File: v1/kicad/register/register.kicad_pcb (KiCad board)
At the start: 2 copper layers, 78.5 x 66.5 mm, 5 parts, among them J3 ASYNC_{out}, U1 74HC173, U2 74HC173, U3 74LS244, U5 LNCPU Type B Connector

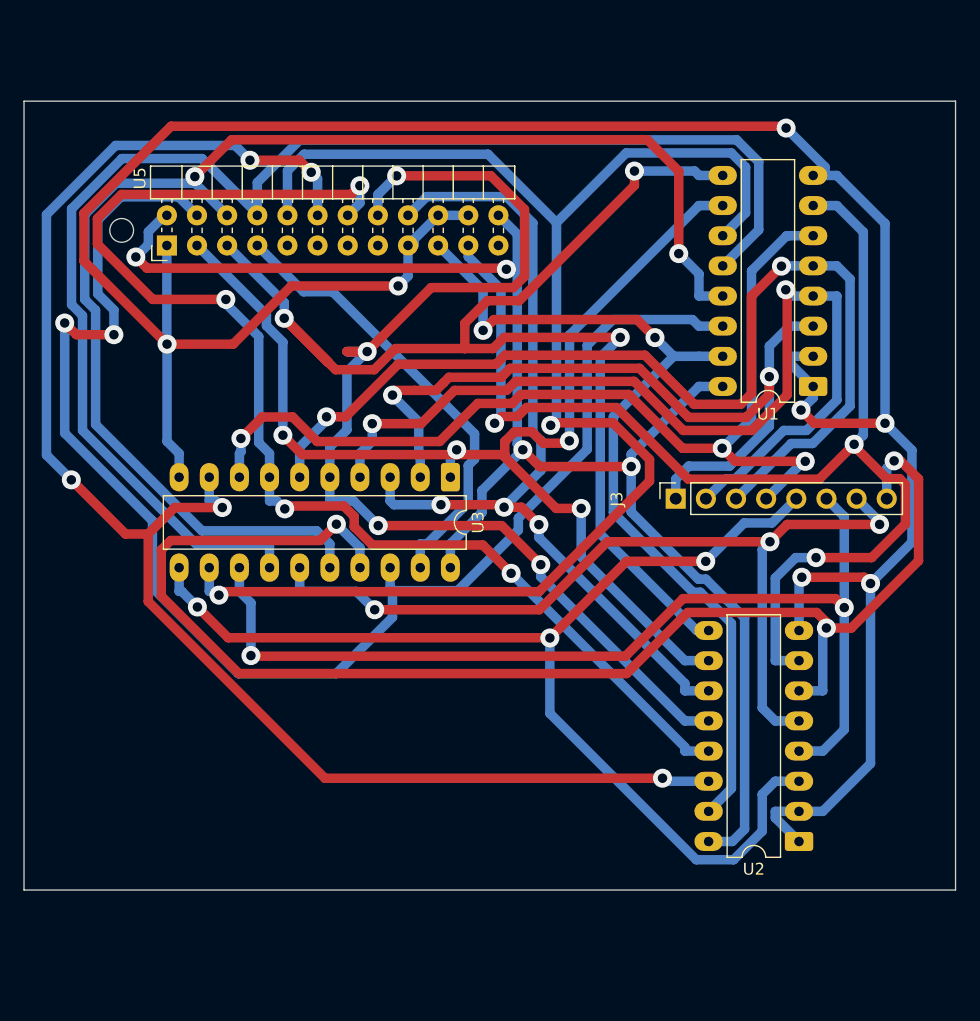
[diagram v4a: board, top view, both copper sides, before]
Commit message: check designs for ALU (partial), SP, Shift register, register
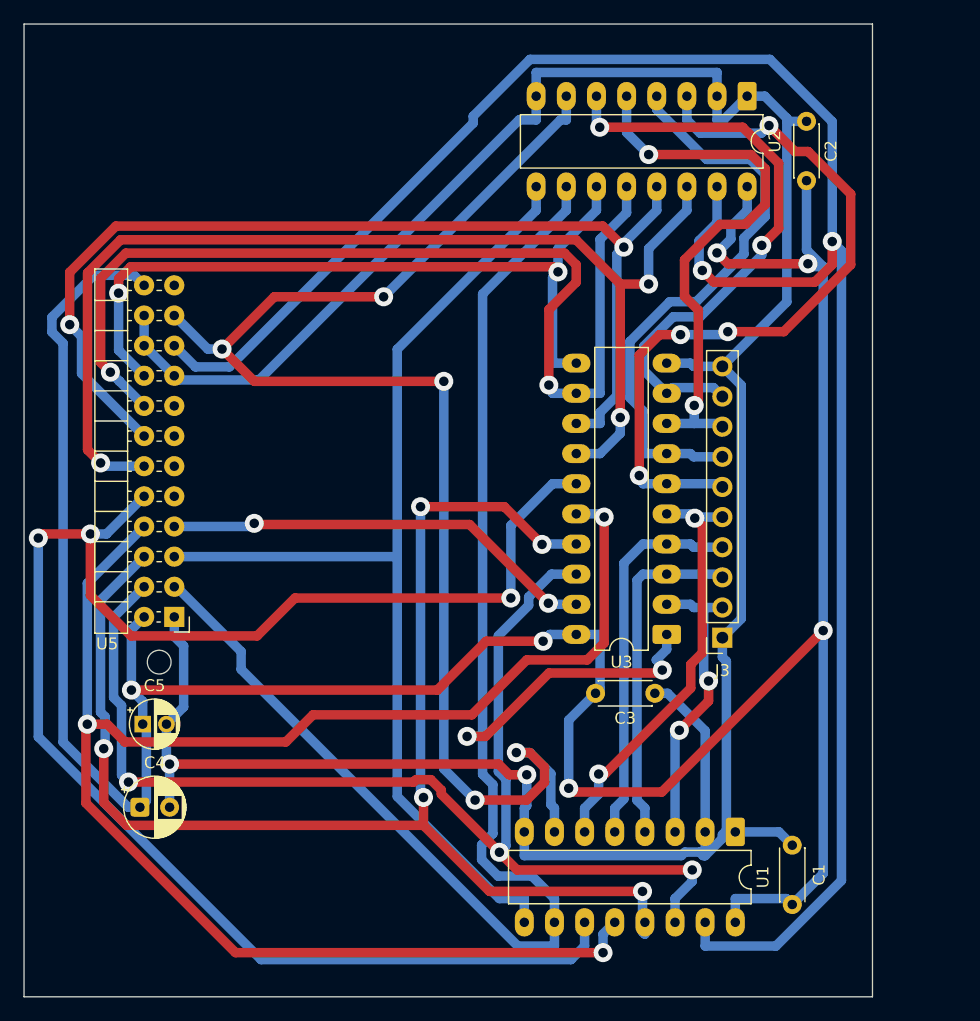
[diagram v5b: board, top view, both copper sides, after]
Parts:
- added C1: 100n, Capacitor_THT:C_Disc_D4.3mm_W1.9mm_P5.00mm, F.Cu at (99.7, 97.7)
- added C2: 100n, Capacitor_THT:C_Disc_D4.3mm_W1.9mm_P5.00mm, F.Cu at (100.9, 36.7)
- added C3: 220n, Capacitor_THT:C_Disc_D4.3mm_W1.9mm_P5.00mm, F.Cu at (83.2, 79.9)
- added C4: 47uF, Capacitor_THT:CP_Radial_D5.0mm_P2.50mm, F.Cu at (44.8, 89.5)
- added C5: 1uF, lncpu:CP_Radial_D4.0mm_P2.00mm-Large-Holes, F.Cu at (45.0, 82.5)
- J3: footprint Connector_PinSocket_2.54mm:PinSocket_1x08_P2.54mm_Vertical -> Connector_PinSocket_2.54mm:PinSocket_1x10_P2.54mm_Vertical
- U1, U2: value 74HC173 -> 74HCT173
- U3: value 74LS244 -> 74HCT541
- moved U2 63.0 mm to (95.9, 29.6), turned to -90 degrees
- moved U1 38.1 mm to (94.9, 91.6), turned to -90 degrees
- moved U5 31.3 mm to (47.7, 73.5), turned to 180 degrees
- moved U3 22.5 mm to (89.2, 74.9), turned to 180 degrees
- moved J3 12.4 mm to (93.8, 75.2), turned to 180 degrees
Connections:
- J3 pad 1: /ASYNC0 -> Net-(U1-GND)
- J3 pad 2: /ASYNC1 -> /ASYNC0
- J3 pad 3: /ASYNC2 -> /ASYNC1
- J3 pad 4: /ASYNC3 -> /ASYNC2
- J3 pad 5: /ASYNC4 -> /ASYNC3
- J3 pad 6: /ASYNC5 -> /ASYNC4
- J3 pad 7: /ASYNC6 -> /ASYNC5
- J3 pad 8: /ASYNC7 -> /ASYNC6
- U3 pad 11: /ASYNC4 -> /DBUS7
- U3 pad 12: /DBUS3 -> /DBUS6
- U3 pad 13: /ASYNC5 -> /DBUS5
- U3 pad 14: /DBUS2 -> /DBUS4
- U3 pad 15: /ASYNC6 -> /DBUS3
- U3 pad 16: /DBUS1 -> /DBUS2
- U3 pad 17: /ASYNC7 -> /DBUS1
- U3 pad 3: /DBUS7 -> /ASYNC1
- U3 pad 4: /ASYNC1 -> /ASYNC2
- U3 pad 5: /DBUS6 -> /ASYNC3
- U3 pad 6: /ASYNC2 -> /ASYNC4
- U3 pad 7: /DBUS5 -> /ASYNC5
- U3 pad 8: /ASYNC3 -> /ASYNC6
- U3 pad 9: /DBUS4 -> /ASYNC7
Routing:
- net Net-(U1-VCC): track 129.5 -> 240.2 mm, vias 4 -> 6
- net Net-(U1-Mr): track 76.8 -> 171.2 mm
- net /ASYNC7: track 116.3 -> 50.5 mm, vias 3 -> 2
- net /ASYNC2: track 87.8 -> 32.0 mm, vias 2 -> 0
- net /ASYNC1: track 81.2 -> 29.0 mm, vias 2 -> 0
- net /ASYNC3: track 83.5 -> 36.0 mm, vias 3 -> 2
- net /ASYNC0: track 67.8 -> 25.1 mm
- net Net-(U1-E2): track 101.9 -> 141.0 mm, vias 4 -> 2
- net /ASYNC5: track 84.8 -> 49.3 mm, vias 2 -> 0
- net /DBUS4: track 130.8 -> 96.8 mm, vias 5 -> 3
- net /ASYNC4: track 97.5 -> 63.6 mm, vias 3 -> 4
- net Net-(U1-E1): track 120.3 -> 91.3 mm, vias 3 -> 0
- net /ASYNC6: track 75.3 -> 47.0 mm, vias 3 -> 2
- net /DBUS0: track 122.7 -> 101.9 mm, vias 2 -> 3
- net /DBUS2: track 117.5 -> 137.8 mm, vias 0 -> 3
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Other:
- board size 78.5 x 66.5 mm -> 71.5 x 82 mm

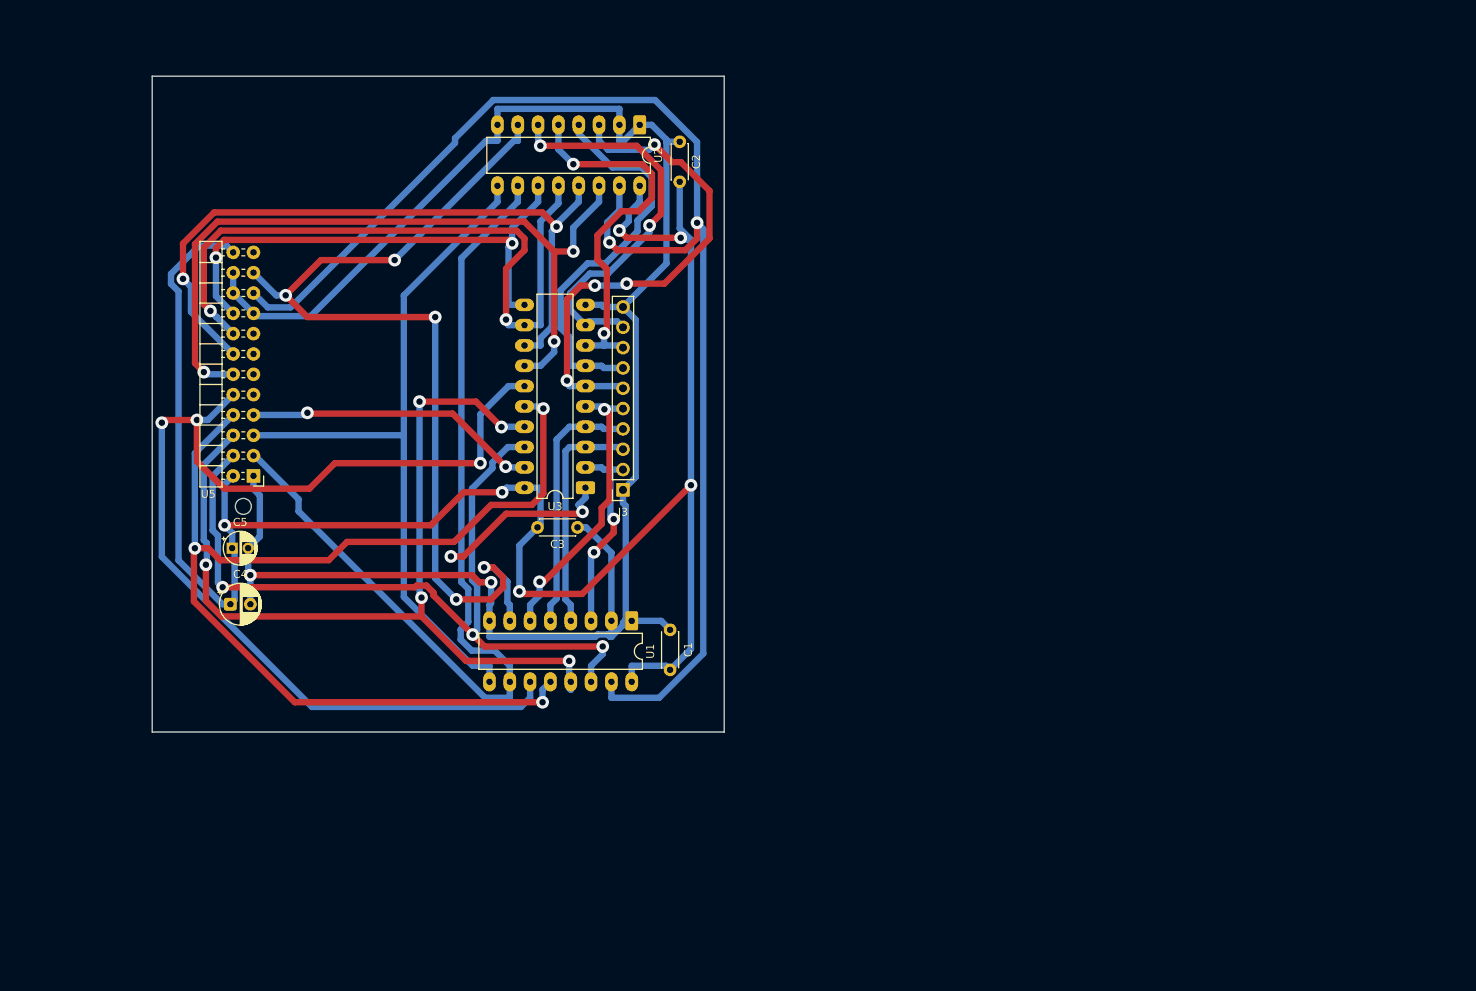
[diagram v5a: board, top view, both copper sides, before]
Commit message: readapt designs for BR, SP, SR, ALU
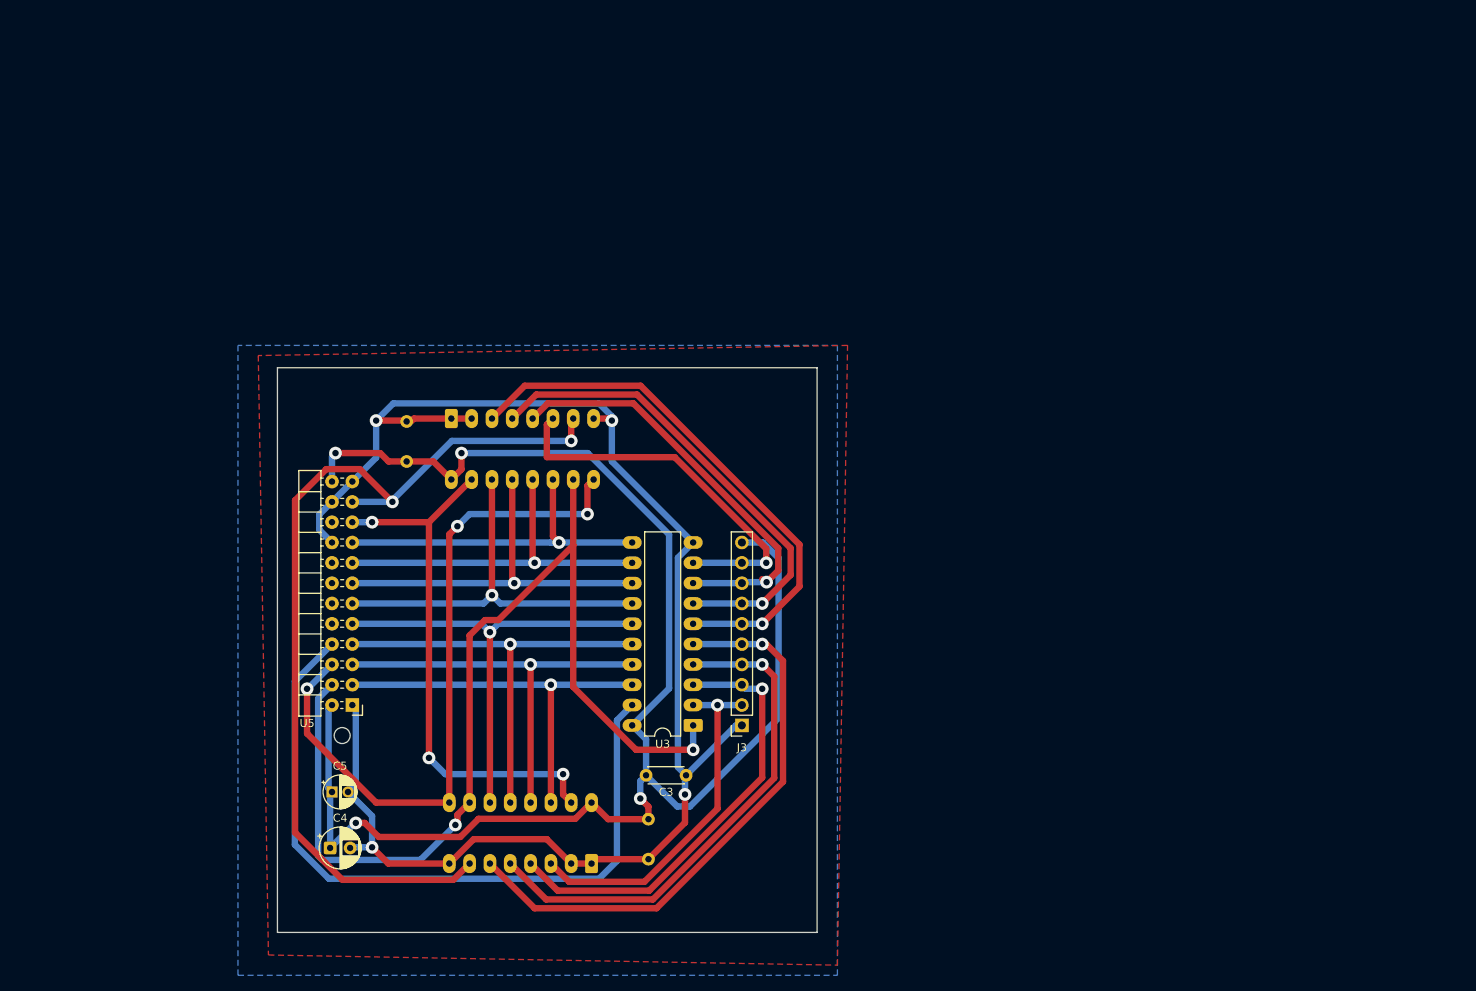
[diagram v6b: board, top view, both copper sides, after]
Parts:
- C1, C2, U1, U2: moved to B.Cu
- moved C2 48.9 mm to (66.8, 71.7)
- moved U2 43.6 mm to (72.4, 66.3)
- moved C3 33.8 mm to (96.7, 110.9)
- moved J3 33.0 mm to (108.7, 104.6)
- moved C4 32.9 mm to (57.2, 120.0)
- moved C5 32.9 mm to (57.5, 113.0)
- moved U3 32.6 mm to (102.6, 104.6)
- moved U5 31.2 mm to (60.0, 102.1)
- moved U1 30.8 mm to (89.9, 121.9), turned to 90 degrees
- moved C1 18.9 mm to (97.0, 116.4), turned to -90 degrees
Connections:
- C1 pad 1: Net-(U1-VCC) -> Net-(J3-VCC)
- C1 pad 2: Net-(U1-GND) -> Net-(J3-GND)
- C2 pad 1: Net-(U1-VCC) -> Net-(J3-VCC)
- C2 pad 2: Net-(U1-GND) -> Net-(J3-GND)
- C3 pad 1: Net-(U1-VCC) -> Net-(J3-VCC)
- C3 pad 2: Net-(U1-GND) -> Net-(J3-GND)
- C4 pad 1: Net-(U1-VCC) -> Net-(J3-VCC)
- C4 pad 2: Net-(U1-GND) -> Net-(J3-GND)
- C5 pad 1: Net-(U1-VCC) -> Net-(J3-VCC)
- C5 pad 2: Net-(U1-GND) -> Net-(J3-GND)
- J3 pad 1: Net-(U1-GND) -> Net-(J3-GND)
- J3 pad 10: Net-(U1-GND) -> Net-(J3-VCC)
- U1 pad 1: Net-(U1-GND) -> Net-(J3-GND)
- U1 pad 16: Net-(U1-VCC) -> Net-(J3-VCC)
- U1 pad 2: Net-(U1-GND) -> Net-(J3-GND)
- U1 pad 8: Net-(U1-GND) -> Net-(J3-GND)
- U2 pad 1: Net-(U1-GND) -> Net-(J3-GND)
- U2 pad 16: Net-(U1-VCC) -> Net-(J3-VCC)
- U2 pad 2: Net-(U1-GND) -> Net-(J3-GND)
- U2 pad 8: Net-(U1-GND) -> Net-(J3-GND)
- U3 pad 10: Net-(U1-GND) -> Net-(J3-GND)
- U3 pad 19: Net-(U3-2OE) -> Net-(U3-G2)
- U3 pad 20: Net-(U1-VCC) -> Net-(J3-VCC)
- U5 pad 1: Net-(U1-GND) -> Net-(J3-GND)
- U5 pad 10: /DBUS3 -> unconnected-(U5-CTRL_{3}-Pad10)
- U5 pad 11: unconnected-(U5-CTRL_{4}-Pad11) -> /DBUS4
- U5 pad 12: /DBUS4 -> unconnected-(U5-CTRL_{4}-Pad12)
- U5 pad 13: unconnected-(U5-CTRL_{5}-Pad13) -> /DBUS5
- U5 pad 14: /DBUS5 -> unconnected-(U5-CTRL_{5}-Pad14)
- U5 pad 15: unconnected-(U5-CTRL_{6}-Pad15) -> /DBUS6
- U5 pad 16: /DBUS6 -> unconnected-(U5-CTRL_{6}-Pad16)
- U5 pad 17: Net-(U1-GND) -> /DBUS7
- U5 pad 18: /DBUS7 -> Net-(J3-GND)
- U5 pad 2: Net-(U1-VCC) -> Net-(J3-VCC)
- U5 pad 20: Net-(U1-GND) -> unconnected-(U5-CLK2-Pad20)
- U5 pad 22: Net-(U1-GND) -> Net-(J3-GND)
- U5 pad 23: unconnected-(U5-CLK2-Pad23) -> Net-(J3-GND)
- U5 pad 24: Net-(U1-VCC) -> Net-(J3-VCC)
- U5 pad 3: Net-(U1-E2) -> /DBUS0
- U5 pad 4: /DBUS0 -> Net-(U1-E2)
- U5 pad 5: Net-(U1-E1) -> /DBUS1
- U5 pad 6: /DBUS1 -> Net-(U1-E1)
- U5 pad 7: Net-(U3-2OE) -> /DBUS2
- U5 pad 8: /DBUS2 -> Net-(U3-G2)
- U5 pad 9: unconnected-(U5-CTRL_{3}-Pad9) -> /DBUS3
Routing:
- net Net-(U1-GND): track 242.0 -> 0.00 mm, vias 2 -> 0
- net Net-(U1-VCC): track 240.2 -> 0.00 mm, vias 6 -> 0
- net Net-(J3-VCC): track 0.00 -> 203.4 mm, vias 0 -> 4
- net Net-(J3-GND): track 0.00 -> 196.7 mm, vias 0 -> 4
- net Net-(U1-Mr): track 171.2 -> 68.2 mm, vias 2 -> 3
- net Net-(U3-G2): track 0.00 -> 90.2 mm
- net /DBUS2: track 137.8 -> 54.8 mm, vias 3 -> 1
- net /DBUS3: track 139.8 -> 57.2 mm, vias 3 -> 1
- net /DBUS1: track 117.1 -> 52.3 mm, vias 5 -> 1
- net /DBUS0: track 101.9 -> 49.7 mm, vias 3 -> 1
- net /DBUS4: track 96.8 -> 50.3 mm, vias 3 -> 1
- net /DBUS6: track 87.9 -> 45.5 mm, vias 2 -> 1
- net /DBUS5: track 89.4 -> 48.0 mm, vias 2 -> 1
- net Net-(U3-2OE): track 36.8 -> 0.00 mm, vias 2 -> 0
- net /ASYNC3: track 36.0 -> 72.7 mm, vias 2 -> 1
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- added copper zone on B.Cu, net Net-(J3-GND)
- added copper zone on F.Cu, net Net-(J3-GND)
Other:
- board size 71.5 x 82 mm -> 67.5 x 70.6 mm
